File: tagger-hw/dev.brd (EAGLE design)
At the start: 72.7 x 62.2 mm, 30 parts, among them IC1 4010D, IC2 LP298XS, J1 SMARTPRJ_MYCON2_USB-MINI-B, X1 MICROSD

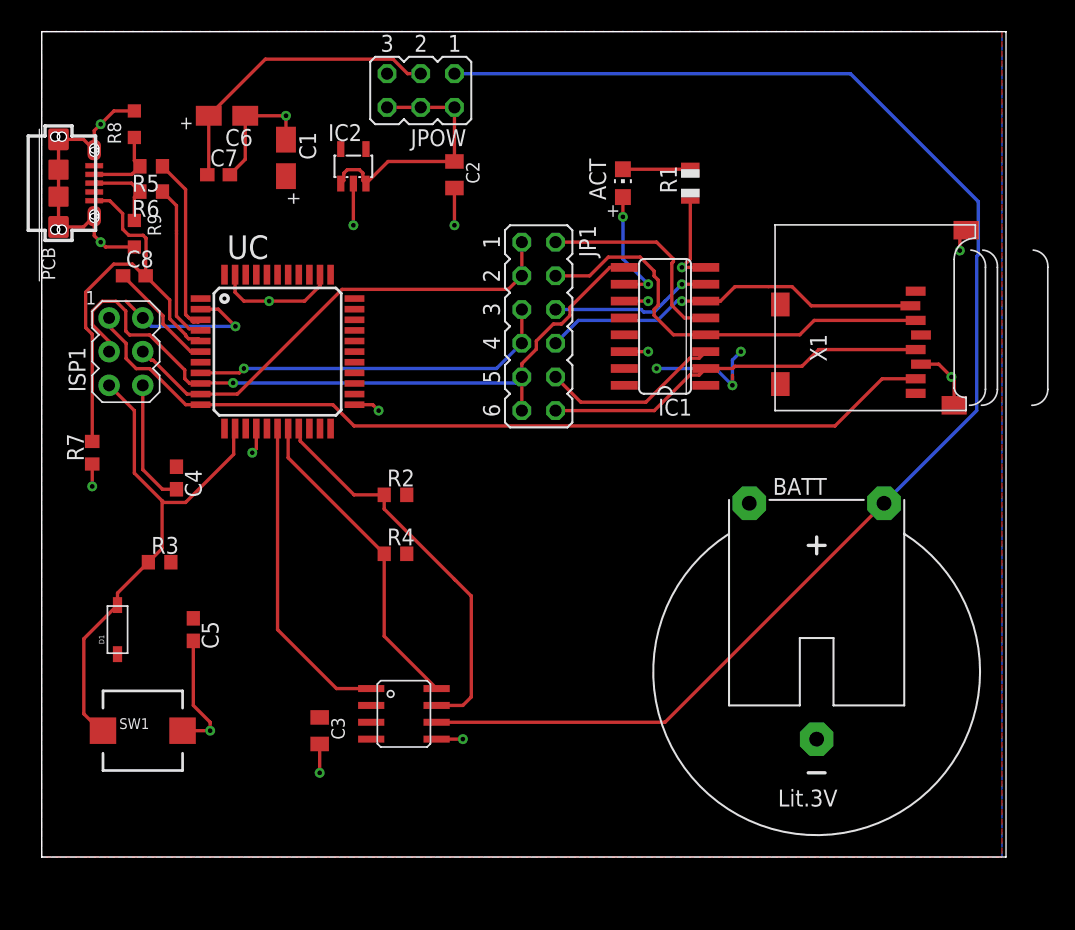
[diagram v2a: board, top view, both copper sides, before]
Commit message: Mostly trace width changes
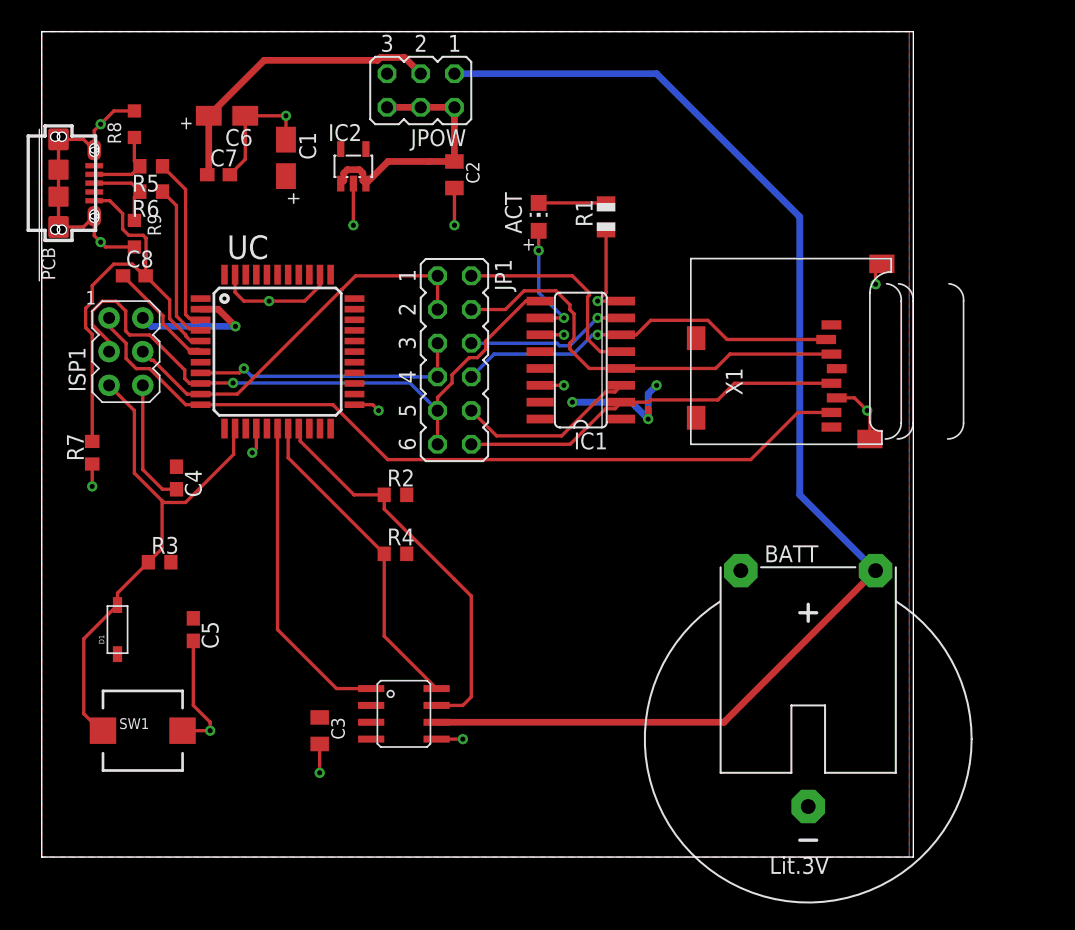
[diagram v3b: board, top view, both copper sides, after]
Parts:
- moved JP1 6.84 mm to (31.1, 37.5)
- moved IC1 6.84 mm to (40.6, 37.5)
- moved R1 6.84 mm to (42.5, 48.3)
- moved ACT 6.84 mm to (37.5, 48.3)
- moved X1 6.84 mm to (48.9, 31.1)
- moved BATT 5.12 mm to (57.8, 8.89)
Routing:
- net VBAT: track 109.7 -> 97.4 mm
- net CS_SD: track 27.7 -> 20.8 mm
- net MOSI: track 36.1 -> 29.8 mm
- net SCK: track 55.3 -> 49.6 mm
- net MISO: track 66.7 -> 61.4 mm
- net +3V3: track 22.0 -> 20.2 mm
- net UCAP: track 8.57 -> 9.31 mm
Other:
- board size 72.7 x 62.2 mm -> 65.7 x 62.2 mm

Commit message: dev_v0 routing/placement lock
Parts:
- removed SW1: (no value), adafruit:PUSHBUTTON_SMD_SJ
- added C9: 0.1uF, adafruit:C0805K
- added F1: MF-MSMF050-2, adafruit:1812
- added R10: 1k, resistor:R0603
- added R11: 100k, resistor:R0603
- added S1: B3F-1002, switch-omron:B3F-10XX
- added SV1: SSA-132-S-T, con-lsta:FE05-1
- added U$1: EXC-31B, dorskyee:XTAL-SM2
- added U$2: MH2029-300Y, dorskyee:C0805
- added UCLK2: DS1347T+, dorskyee:8_TDFN-EP
- added X2, X3: 22-23-2021, con-molex:22-23-2021
- D1: value (none) -> 1N4148W-7-F
- JP1, JPOW: value (none) -> HDR100IMP40M-G-V-TH
- moved R4 7.01 mm to (19.7, 22.2), turned to 270 degrees
- moved BATT 6.75 mm to (52.7, 13.3)
- moved R2 6.48 mm to (20.3, 26.0), turned to 270 degrees
- moved C1 6.25 mm to (24.1, 50.2)
- moved C7 6.25 mm to (19.1, 48.9)
- moved C6 6.25 mm to (19.7, 53.3)
- moved IC2 4.45 mm to (27.9, 52.1)
- moved R6 0.63 mm to (8.26, 49.5)
- renumbered UCLK to UCLK1
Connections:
- removed net VBUS_L: J1.P1
- new net CS_RTC: UC.28, UCLK2.P$1
- new net PPS: SV1.1, UC.30
- new net RTC_X1: U$1.P$2, UCLK2.P$8
- new net RTC_X2: U$1.P$1, UCLK2.P$7
- new net RX: SV1.2, UC.20
- new net TRIG_H: R10.1, X2.1
- new net TRIG_L: R11.2, UC.29, X2.2
- new net TX: SV1.3, UC.21
- new net VBUS_F: F1.1, J1.P1
- net +3V3: now also C9.1, R10.2, SV1.5, UCLK2.P$6
- net GND: now also C9.2, R11.1, S1.3, S1.4, SV1.4, U$2.1, UCLK2.P$4, X3.2; no longer SW1.P$1
- net MISO: now also UCLK2.P$2
- net MOSI: now also UCLK2.P$3
- net RESET: now also S1.1, S1.2; no longer SW1.P$2
- net UGND: now also U$2.2
- net VBUS: now also F1.2, UC.7
- net VEXT: now also X3.1
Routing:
- net PPS: track 0.00 -> 40.9 mm, vias 0 -> 1
- net RX: track 0.00 -> 36.3 mm, vias 0 -> 1
- net TRIG_L: track 0.00 -> 32.1 mm, vias 0 -> 1
- net TX: track 0.00 -> 31.0 mm, vias 0 -> 1
- net MOSI: track 29.8 -> 52.1 mm, vias 0 -> 1
- net CS_RTC: track 0.00 -> 19.4 mm, vias 0 -> 2
- net GND: track 94.0 -> 113.3 mm, vias 17 -> 21
- net VEXT: track 0.00 -> 18.4 mm
- net VBUS: track 22.8 -> 37.6 mm, vias 0 -> 2
- net VBUS_F: track 0.00 -> 14.7 mm
- net MISO: track 61.4 -> 71.8 mm
- net VBAT: track 97.4 -> 88.7 mm
- net RESET: track 39.8 -> 44.5 mm
- net VCC: track 19.9 -> 15.9 mm
- net TRIG_H: track 0.00 -> 3.26 mm
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- added copper zone on layer 16, net +3V3
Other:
- board text added: "12/28/2017"
- board text added: "Evan Dorsky"
- board text added: "Film Tagger dev_v0"

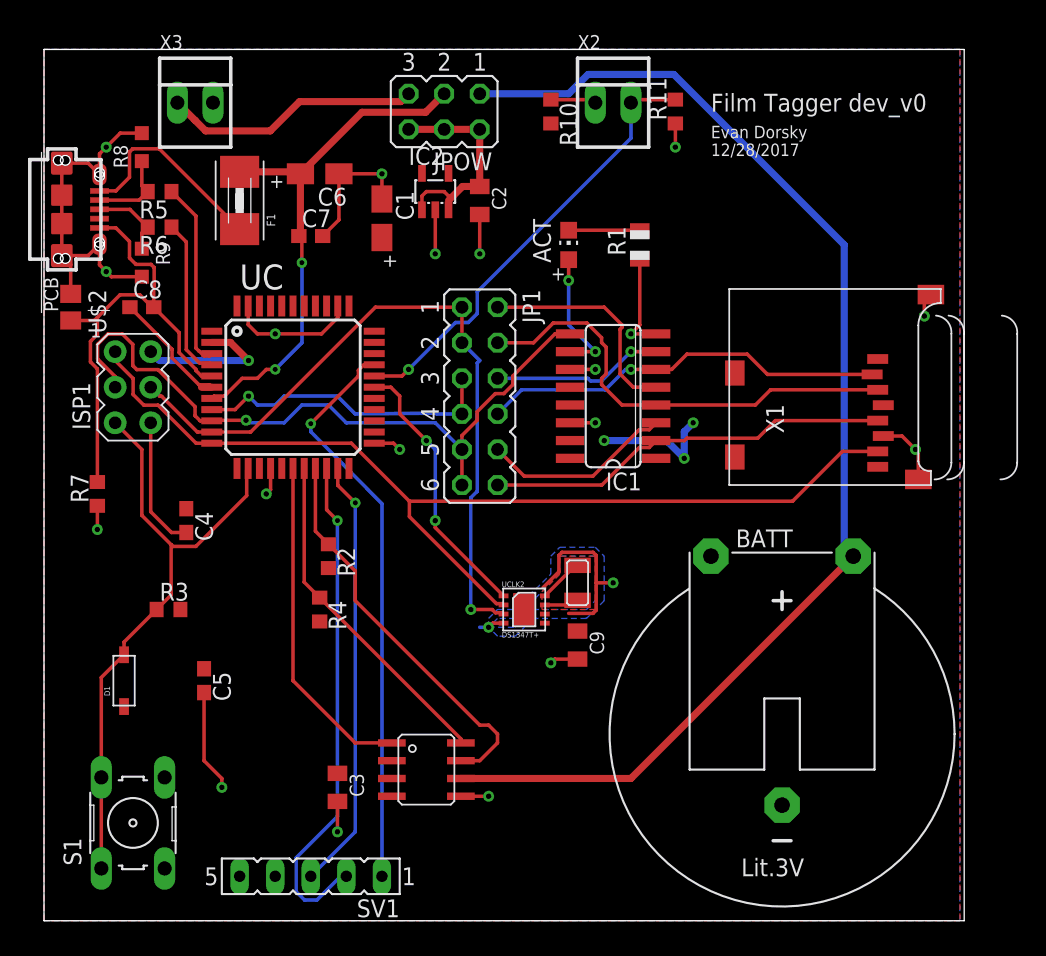
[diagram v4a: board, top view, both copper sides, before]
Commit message: Just kidding, add more buttons and LEDs
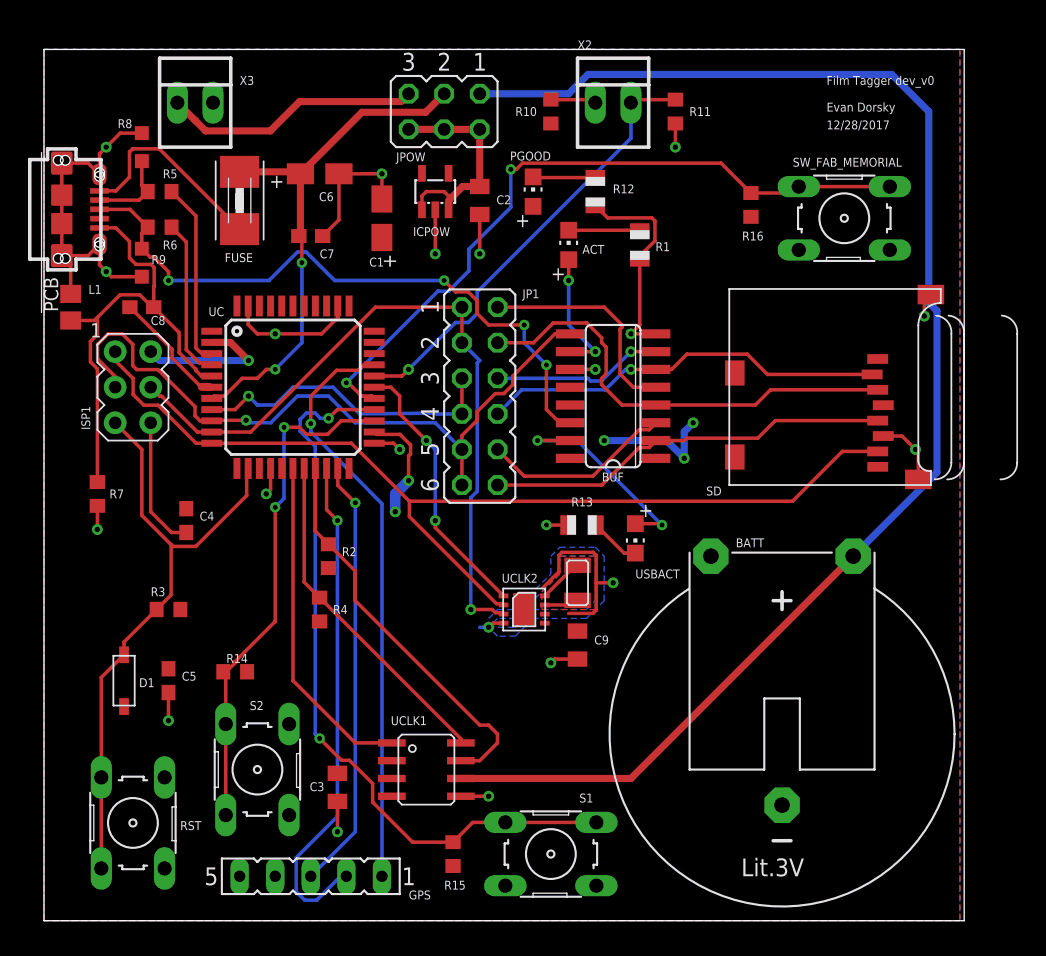
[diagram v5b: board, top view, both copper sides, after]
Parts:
- added PGOOD, USBACT: GREEN, adafruit:CHIP-LED0805
- added R12, R13: 1K, adafruit:R0805
- added R14, R15, R16: 10k, resistor:R0603
- added RST, S2, SW_FAB_MEMORIAL: B3F-1002, switch-omron:B3F-10XX
- moved S1 29.9 mm to (36.2, 4.76), turned to 0 degrees
- moved C5 2.54 mm to (8.89, 17.1)
- renumbered F1 to FUSE, IC1 to BUF, IC2 to ICPOW, SV1 to GPS, U$2 to L1, X1 to SD
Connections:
- new net +3V3_D: PGOOD.C, R12.2
- new net BTN1: R14.1, S2.1, S2.2, UC.25
- new net BTN2: R15.1, S1.1, S1.2, UC.26
- new net BTN3: R16.1, SW_FAB_MEMORIAL.1, SW_FAB_MEMORIAL.2, UC.27
- new net D+_BUF: BUF.15, USBACT.A
- new net D+_BUF_D: R13.2, USBACT.C
- net +3V3: now also PGOOD.A, R14.2, R15.2, R16.2
- net D+: now also BUF.14
- net GND: now also R12.1, R13.1, RST.3, RST.4, S2.3, S2.4, SW_FAB_MEMORIAL.3, SW_FAB_MEMORIAL.4; no longer BUF.14
- net RESET: now also RST.1, RST.2; no longer S1.1, S1.2
- net VBUS: now also FUSE.1, J1.P1; no longer C6.+, C7.1, FUSE.2, JPOW.3, UC.7
- net VBUS_F: now also C6.+, C7.1, FUSE.2, JPOW.3, UC.7; no longer FUSE.1, J1.P1
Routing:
- net BTN2: track 0.00 -> 53.4 mm, vias 0 -> 2
- net BTN3: track 0.00 -> 51.3 mm, vias 0 -> 2
- net D+: track 5.68 -> 46.6 mm, vias 0 -> 4
- net BTN1: track 0.00 -> 36.7 mm, vias 0 -> 2
- net VBUS_F: track 14.7 -> 37.6 mm, vias 0 -> 2
- net VBUS: track 37.6 -> 14.7 mm, vias 2 -> 0
- net D+_BUF: track 0.00 -> 15.7 mm, vias 0 -> 2
- net VBAT: track 88.7 -> 102.8 mm
- net +3V3: track 19.5 -> 27.6 mm, vias 4 -> 6
- net +3V3_D: track 0.00 -> 4.47 mm
- net D+_BUF_D: track 0.00 -> 3.64 mm
- net GND: track 113.3 -> 115.6 mm
- net PPS: track 40.9 -> 41.8 mm
- net CS_SD: track 21.9 -> 22.4 mm
- net SCK: track 50.7 -> 51.2 mm

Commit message: Minor name changes
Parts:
- renumbered U$1 to X1, X2 to J2, X3 to J3
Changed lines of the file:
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@@
 <attribute name="VALUE" x="36.2" y="20.685" size="0.635" layer="27" font="vector" rot="R270"/>
 </element>
-<element name="U$1" library="dorskyee" package="XTAL-SM2" value="EXC-31B" x="38.1" y="24.13" smashed="yes" rot="R90"/>
-<element name="X2" library="con-molex" library_urn="urn:adsk.eagle:library:165" package="22-23-2021" value="22-23-2021" x="40.64" y="58.42" smashed="yes">
+<element name="X1" library="dorskyee" package="XTAL-SM2" value="EXC-31B" x="38.1" y="24.13" smashed="yes" rot="R90"/>
+<element name="J2" library="con-molex" library_urn="urn:adsk.eagle:library:165" package="22-23-2021" value="22-23-2021" x="40.64" y="58.42" smashed="yes">
 <attribute name="MF" value="MOLEX" x="40.64" y="58.42" size="1.778" layer="27" display="off"/>
 <attribute name="MPN" value="22-23-2021" x="40.64" y="58.42" size="1.778" layer="27" display="off"/>
@@
 <attribute name="VALUE" x="46.99" y="57.15" size="0.635" layer="27" font="vector" rot="R90"/>
 </element>
-<element name="X3" library="con-molex" library_urn="urn:adsk.eagle:library:165" package="22-23-2021" value="22-23-2021" x="10.795" y="58.42" smashed="yes">
+<element name="J3" library="con-molex" library_urn="urn:adsk.eagle:library:165" package="22-23-2021" value="22-23-2021" x="10.795" y="58.42" smashed="yes">
 <attribute name="MF" value="MOLEX" x="10.795" y="58.42" size="1.778" layer="27" display="off"/>
 <attribute name="MPN" value="22-23-2021" x="10.795" y="58.42" size="1.778" layer="27" display="off"/>
@@
 <wire x1="45.085" y1="56.935" x2="45.085" y2="55.245" width="0.254" layer="1"/>
 <via x="45.085" y="55.245" extent="1-16" drill="0.381"/>
-<contactref element="X3" pad="2"/>
+<contactref element="J3" pad="2"/>
 <wire x1="36.195" y1="18.415" x2="36.465" y2="18.685" width="0.254" layer="1"/>
 <wire x1="36.465" y1="18.685" x2="38.1" y2="18.685" width="0.254" layer="1"/>
@@
 <signal name="VEXT">
 <contactref element="JPOW" pad="5"/>
-<contactref element="X3" pad="1"/>
+<contactref element="J3" pad="1"/>
 <wire x1="9.525" y1="58.42" x2="10.795" y2="57.15" width="0.508" layer="1"/>
 <wire x1="10.795" y1="57.15" x2="10.79625625" y2="57.15" width="0.508" layer="1"/>
@@
 <signal name="RTC_X2">
 <contactref element="UCLK2" pad="P$7"/>
-<contactref element="U$1" pad="P$1"/>
+<contactref element="X1" pad="P$1"/>
 <wire x1="35.765" y1="22.55" x2="37.77" y2="22.55" width="0.254" layer="1"/>
 <wire x1="37.77" y1="22.55" x2="38.1" y2="22.88" width="0.254" layer="1"/>
@@
 <signal name="RTC_X1">
 <contactref element="UCLK2" pad="P$8"/>
-<contactref element="U$1" pad="P$2"/>
+<contactref element="X1" pad="P$2"/>
 <wire x1="35.765" y1="23.2" x2="37.945" y2="25.38" width="0.254" layer="1"/>
 <wire x1="37.945" y1="25.38" x2="38.1" y2="25.38" width="0.254" layer="1"/>
@@
 </signal>
 <signal name="TRIG_L">
-<contactref element="X2" pad="2"/>
+<contactref element="J2" pad="2"/>
 <contactref element="R11" pad="2"/>
 <contactref element="UC" pad="29"/>
@@
 </signal>
 <signal name="TRIG_H">
-<contactref element="X2" pad="1"/>
+<contactref element="J2" pad="1"/>
 <contactref element="R10" pad="1"/>
 <wire x1="39.37" y1="58.42" x2="39.155" y2="58.635" width="0.254" layer="1"/>

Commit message: More renaming
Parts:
- ICPOW: value LP298XS -> CAT6219-330TDGT3
- renumbered J1 to JUSB
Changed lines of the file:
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@@
 <attribute name="VALUE" x="29.215" y="52.435" size="0.635" layer="27" font="vector" rot="R270"/>
 </element>
-<element name="ICPOW" library="adafruit" package="SOT23-5L" value="LP298XS" x="27.94" y="52.07" smashed="yes">
+<element name="ICPOW" library="adafruit" package="SOT23-5L" value="CAT6219-330TDGT3" x="27.94" y="52.07" smashed="yes">
 <attribute name="NAME" x="26.3525" y="48.895" size="0.635" layer="25" font="vector"/>
 <attribute name="VALUE" x="26.035" y="48.641" size="0.635" layer="27" font="vector"/>
@@
 <attribute name="VALUE" x="32.004" y="63.627" size="0.635" layer="27" font="vector" ratio="10" rot="R180"/>
 </element>
-<element name="J1" library="dorskyee" package="SMARTPRJ_CON2_USB_MICRO_B_AT" value="SMARTPRJ_MYCON2_USB-MINI-B" x="1.27" y="50.8" smashed="yes" rot="R270"/>
+<element name="JUSB" library="dorskyee" package="SMARTPRJ_CON2_USB_MICRO_B_AT" value="SMARTPRJ_MYCON2_USB-MINI-B" x="1.27" y="50.8" smashed="yes" rot="R270"/>
 <element name="R5" library="resistor" library_urn="urn:adsk.eagle:library:348" package="R0603" package3d_urn="urn:adsk.eagle:package:26057/1" value="22" x="8.255" y="52.07" smashed="yes" rot="R180">
 <attribute name="NAME" x="9.525" y="53.6575" size="0.635" layer="25" font="vector" rot="R180"/>
@@
 <via x="20.955" y="6.35" extent="1-16" drill="0.381"/>
 <contactref element="BATT" pad="-"/>
-<contactref element="J1" pad="S6"/>
-<contactref element="J1" pad="S5"/>
-<contactref element="J1" pad="S4"/>
-<contactref element="J1" pad="S3"/>
-<contactref element="J1" pad="S2"/>
-<contactref element="J1" pad="S1"/>
+<contactref element="JUSB" pad="S6"/>
+<contactref element="JUSB" pad="S5"/>
+<contactref element="JUSB" pad="S4"/>
+<contactref element="JUSB" pad="S3"/>
+<contactref element="JUSB" pad="S2"/>
+<contactref element="JUSB" pad="S1"/>
 <contactref element="C7" pad="2"/>
 <contactref element="C6" pad="-"/>
@@
 </signal>
 <signal name="D-">
-<contactref element="J1" pad="P2"/>
+<contactref element="JUSB" pad="P2"/>
 <contactref element="R5" pad="2"/>
 <contactref element="R8" pad="1"/>
@@
 </signal>
 <signal name="D+">
-<contactref element="J1" pad="P3"/>
+<contactref element="JUSB" pad="P3"/>
 <contactref element="R6" pad="2"/>
 <contactref element="R9" pad="1"/>
@@
 </signal>
 <signal name="UGND">
-<contactref element="J1" pad="P5"/>
+<contactref element="JUSB" pad="P5"/>
 <contactref element="C8" pad="2"/>
 <contactref element="UC" pad="5"/>
@@
 </signal>
 <signal name="VBUS">
-<contactref element="J1" pad="P1"/>
+<contactref element="JUSB" pad="P1"/>
 <contactref element="FUSE" pad="1"/>
 <wire x1="6.104" y1="54.9028125" x2="6.3271875" y2="55.126" width="0.254" layer="1"/>
